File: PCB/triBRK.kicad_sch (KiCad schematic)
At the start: 11 parts, among them SW1 SW_Push, SW2 SW_Push, SW3 SW_Push, SW4 SW_Push, SW5 SW_Push, U1 YAAJ_BluePill_Part_Like

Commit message: Small changes
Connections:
- net +3.3V: no longer U1.38 (3V3)
- no-connect marks 29 -> 30
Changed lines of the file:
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@@
   (junction (at 52.07 64.77) (diameter 0) (color 0 0 0 0)
   )
+  (no_connect (at 106.68 67.31))
   (no_connect (at 66.04 74.93))
   (no_connect (at 66.04 69.85))
@@
     (stroke (width 0) (type default) (color 0 0 0 0))
   )
-  (wire (pts (xy 106.68 67.31) (xy 110.49 67.31))
-    (stroke (width 0) (type default) (color 0 0 0 0))
-  )
   (wire (pts (xy 57.15 104.14) (xy 57.15 105.41))
     (stroke (width 0) (type default) (color 0 0 0 0))
@@
     (pin "1")
   )
-  (symbol (lib_id "power:+3.3V") (at 110.49 67.31 0) (unit 1)
-    (in_bom yes) (on_board yes) (fields_autoplaced)
-    (property "Reference" "#PWR0102" (id 0) (at 110.49 71.12 0)
-      (effects (font (size 1.27 1.27)) hide)
-    )
-    (property "Value" "+3.3V" (id 1) (at 110.49 62.23 0))
-    (property "Footprint" "" (id 2) (at 110.49 67.31 0)
-      (effects (font (size 1.27 1.27)) hide)
-    )
-    (property "Datasheet" "" (id 3) (at 110.49 67.31 0)
-      (effects (font (size 1.27 1.27)) hide)
-    )
-    (pin "1")
-  )
   (symbol (lib_id "Switch:SW_Push") (at 35.56 87.63 0) (unit 1)
     (in_bom yes) (on_board yes) (fields_autoplaced)
@@
       (reference "#PWR0101") (unit 1) (value "GND") (footprint "")
     )
-    (path "/7977b3bb-14cb-4bab-a1b9-c46e3be4ea32"
-      (reference "#PWR0102") (unit 1) (value "+3.3V") (footprint "")
-    )
     (path "/105a4075-0773-4e27-a911-bba5e0316a92"

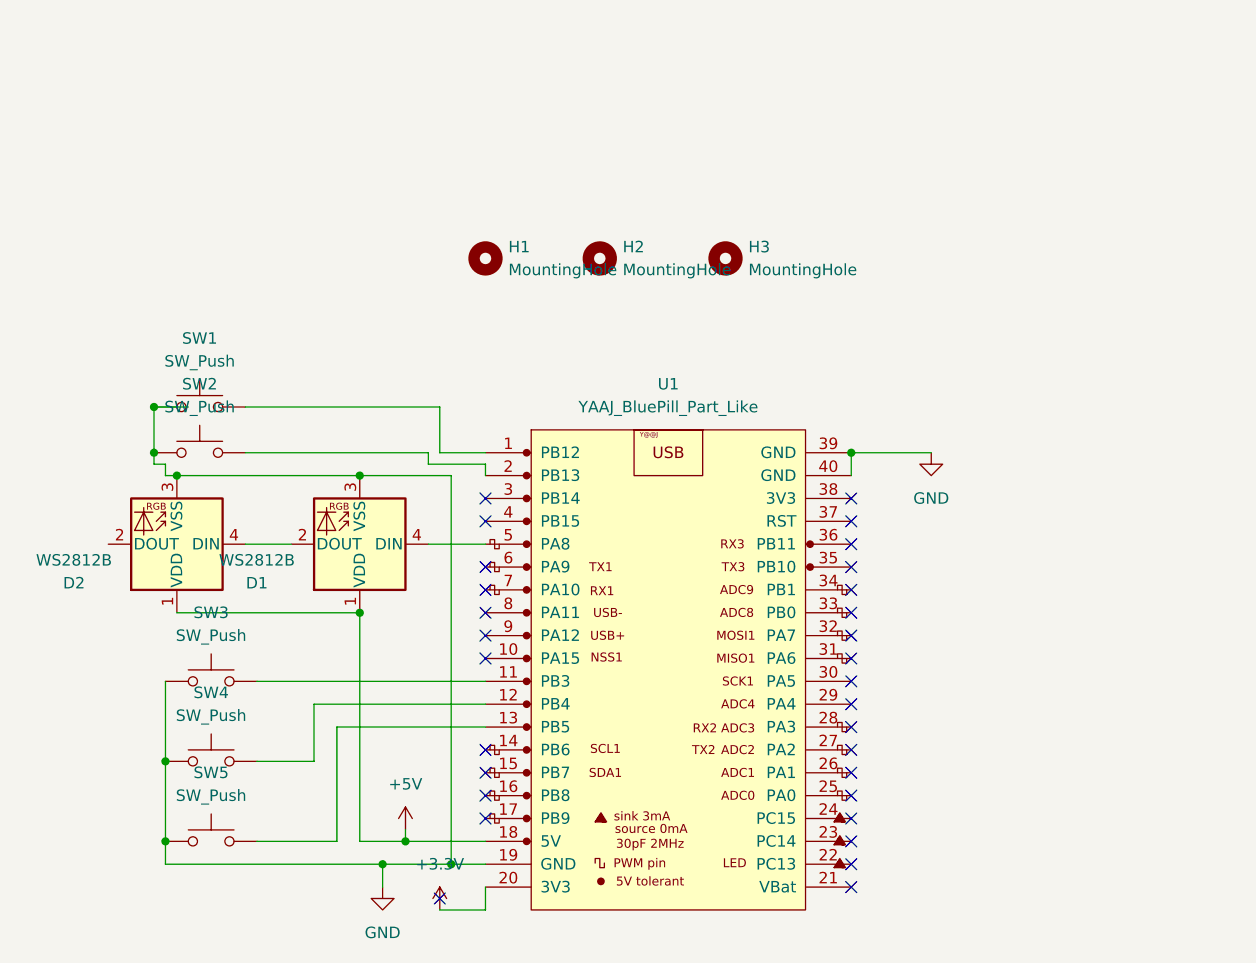
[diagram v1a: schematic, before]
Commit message: Changed holes specs and optimized wiring, nicer schematic also
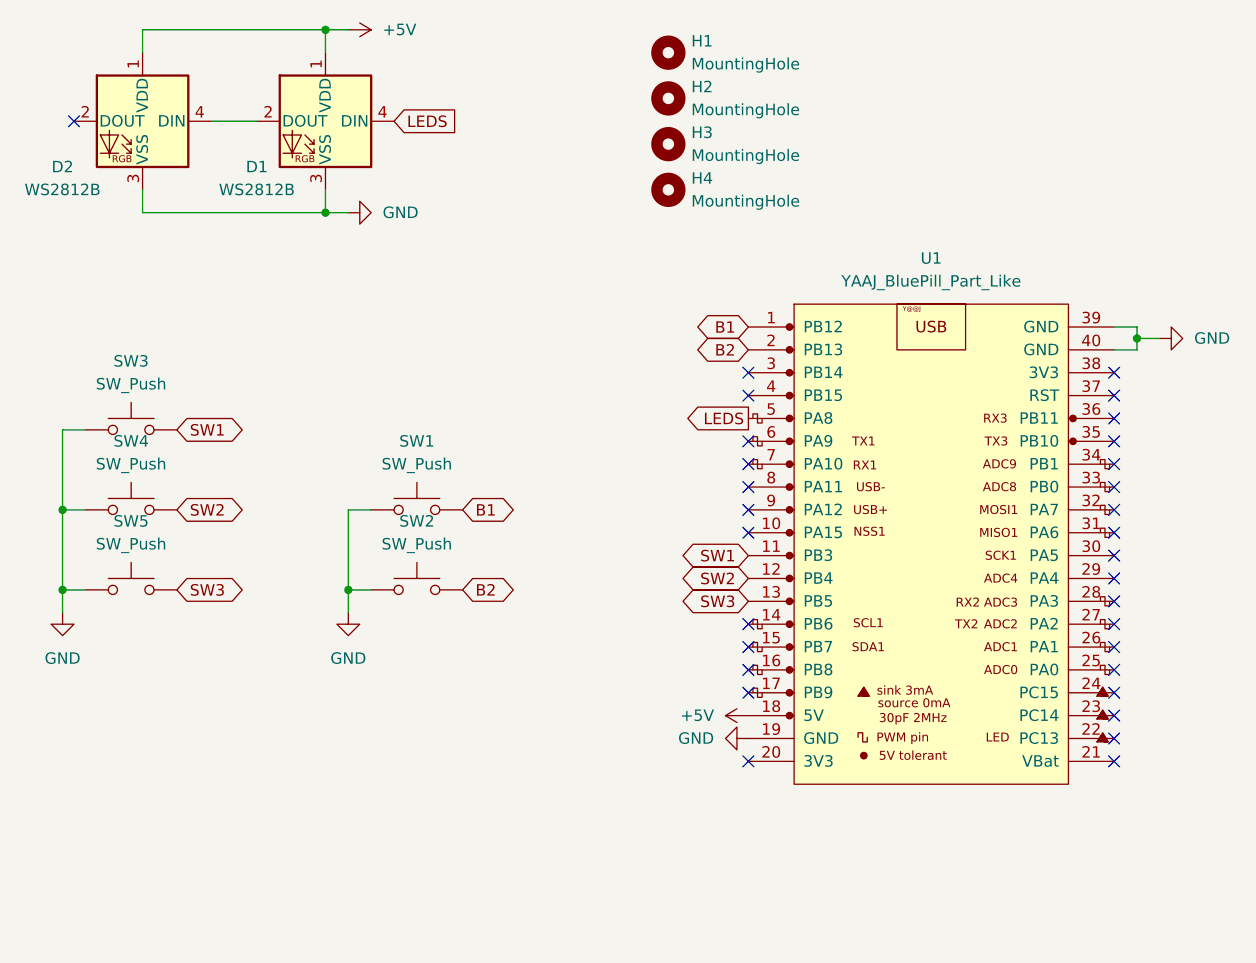
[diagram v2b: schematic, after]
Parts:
- added H4: MountingHole, MountingHole:MountingHole_2.2mm_M2_Pad_Via, symbol Mechanical:MountingHole
- H1, H2, H3: footprint MountingHole:MountingHole_2.2mm_M2_ISO7380 -> MountingHole:MountingHole_2.2mm_M2_Pad_Via
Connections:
- net B1: now reaches SW1.2, U1.1 (PB12)
- net SW1: now reaches SW3.2, U1.11 (PB3)
- net SW2: now reaches SW4.2, U1.12 (PB4)
- net SW3: now reaches SW5.2, U1.13 (PB5)
- net B2: now reaches SW2.2, U1.2 (PB13)
- net LEDS: now reaches D1.4 (DIN), U1.5 (PA8)
- net +3.3V: no longer names the net of U1.20 (3V3)
- no-connect marks 30 -> 31
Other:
- moved on the sheet: D1, D2, H1, H2, H3, SW1, SW2, SW3, SW4, SW5, U1
